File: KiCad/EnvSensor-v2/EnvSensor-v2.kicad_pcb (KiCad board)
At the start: 2 copper layers, 120 x 100 mm, 162 parts, among them J1 JTAG, J10 Conn_01x02, J2 Conn_01x02, J3 USB_B_Micro, J4 Conn_01x02, J5 Micro_SD_Card_Det, J6 Conn_01x02, J7 I2C, J8 HPMA115C0-003, J9 Conn_01x02, P1 USB_C_Plug_USB2.0, Q1 IRLML2502, Q2 Si3407DV, Q3 AUiRLR3110Z, Q4 AO6804A, SW1 SW_Push, SW2 Reset, SW3 SW_Push, SW4 SW_Push, SW5 SW_Push, SW6 Start, U1 STM32L451RCT6, U10 LTC3440, U11 MCP1826S-5.0, U12 MCP1825S-3.3, U13 ESP-12S, U2 E-Ink_Waveshare_4.2, U3 SCD30, U4 SCD40, U5 BME280, U6 AP9101CK, U7 MCP73843-4.2, U8 BME280-Module, U9 LM2735XMF, Y1 16Hz, Y2 32768/12.5pF

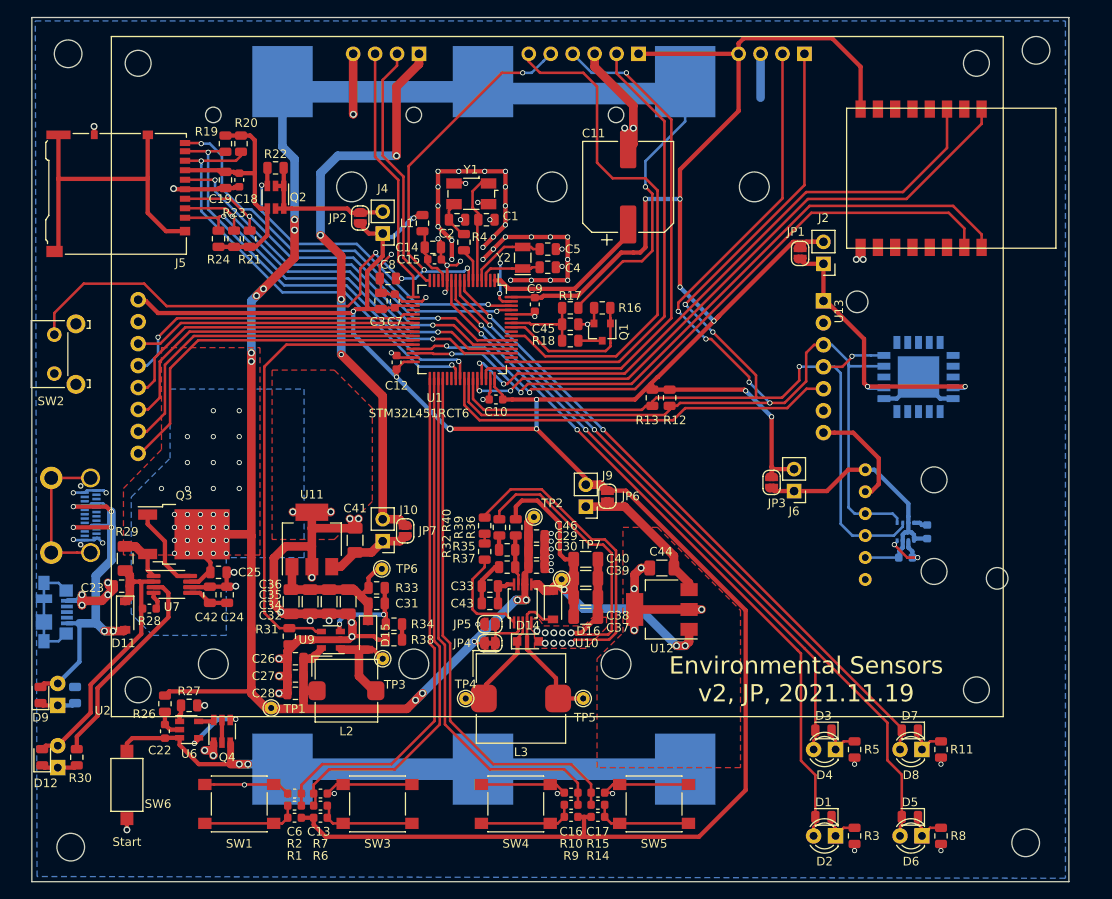
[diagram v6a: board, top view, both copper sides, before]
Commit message: Optimising ground pane
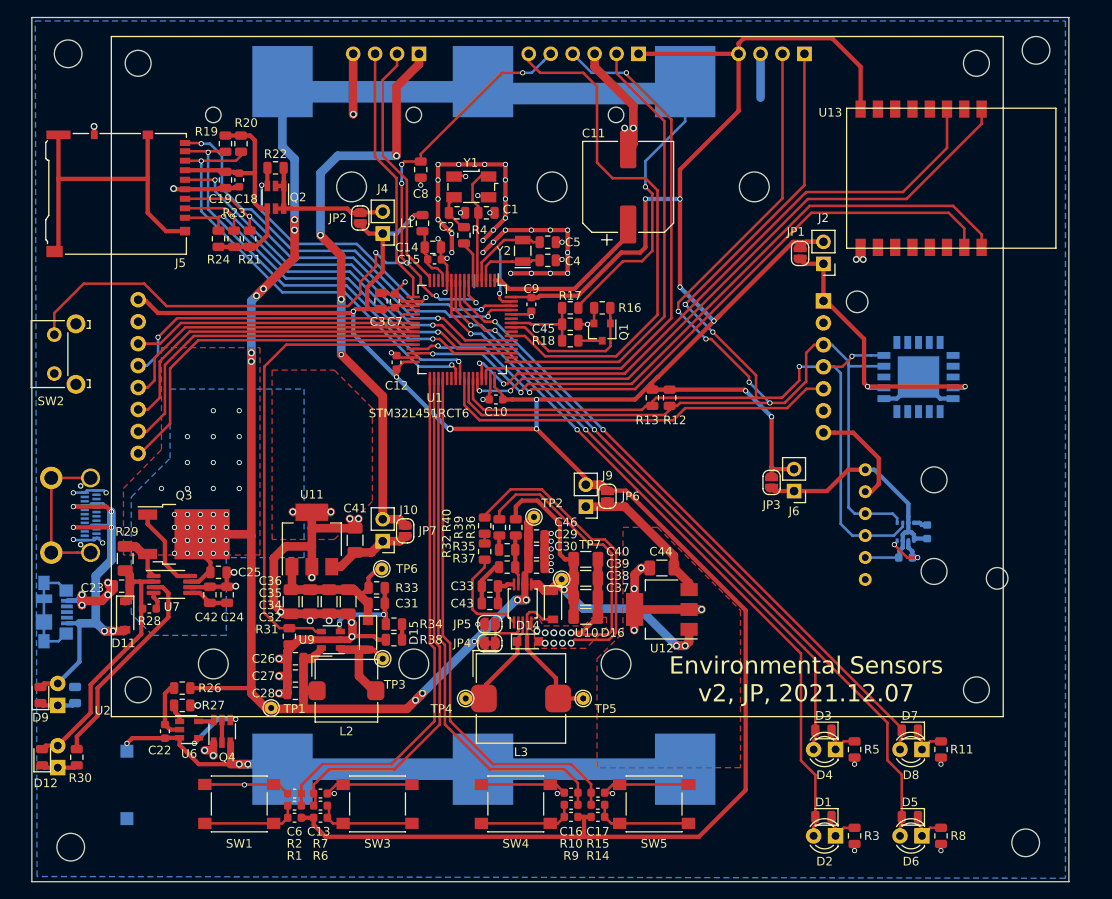
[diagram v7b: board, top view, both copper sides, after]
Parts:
- SW6: moved to B.Cu
- moved C8 13.2 mm to (95.0, 67.6), turned to 90 degrees
- moved R26 2.69 mm to (67.4, 127.6), turned to 180 degrees
- moved C1 0.80 mm to (102.6, 72.6)
- moved C2 0.80 mm to (99.2, 72.6)
- moved C4 0.80 mm to (109.7, 78.1)
- moved Y1 0.80 mm to (100.8, 69.6)
- moved C5 0.80 mm to (109.7, 76.0)
- moved R27 0.80 mm to (67.4, 129.6)
- moved R4 0.80 mm to (100.0, 75.2)
- moved Y2 0.80 mm to (106.8, 77.0)
- moved C9 0.40 mm to (107.8, 83.2)
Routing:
- net Net-(C22-Pad1): track 3.42 -> 6.85 mm
- net +BATT: track 245.1 -> 241.8 mm
- net GND: track 421.2 -> 418.1 mm, vias 107 -> 105
- net NRST: track 95.9 -> 98.6 mm, vias 5 -> 7
- net Net-(C4-Pad1): track 7.34 -> 8.14 mm
- net Net-(C5-Pad1): track 9.17 -> 9.97 mm
- net Net-(R4-Pad1): track 3.72 -> 4.52 mm
- net Net-(C1-Pad1): track 13.0 -> 13.8 mm
- net SDIO_DETECT: track 48.1 -> 48.8 mm
- net LED_1: track 81.8 -> 82.5 mm
- net LED_4: track 75.3 -> 76.0 mm
- net LED_3: track 85.5 -> 86.2 mm
- net LED_2: track 71.6 -> 72.3 mm
- net +3V3: track 372.1 -> 372.8 mm
- net -BATT: vias 2 -> 3
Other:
- board text added: "Environmental Sensors v2, JP, 2021.12.07"
- board text removed: "Environmental Sensors v2, JP, 2021.11.19"

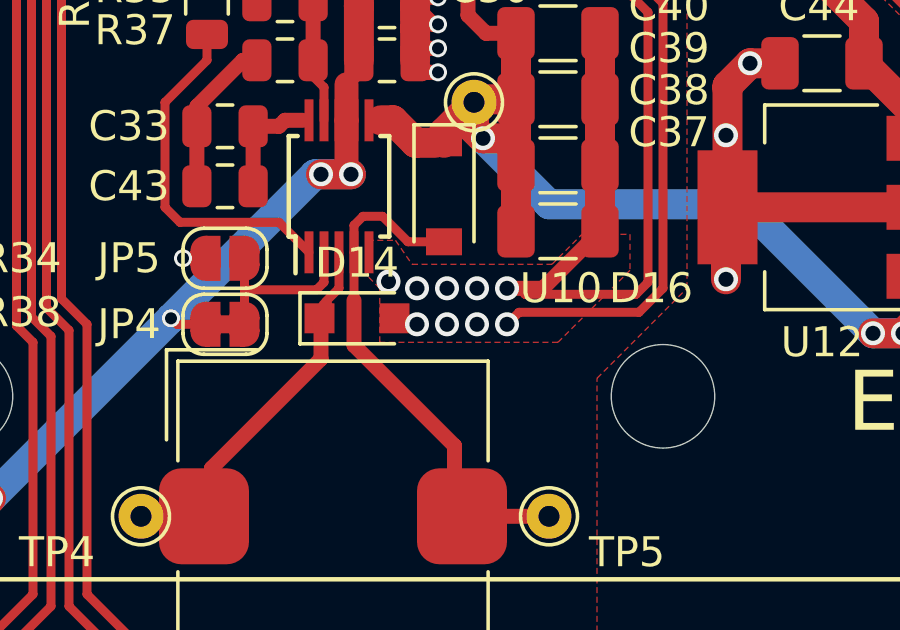
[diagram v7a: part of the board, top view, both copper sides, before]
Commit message: STM32CubeIDE/EnvSensorV2 introduced
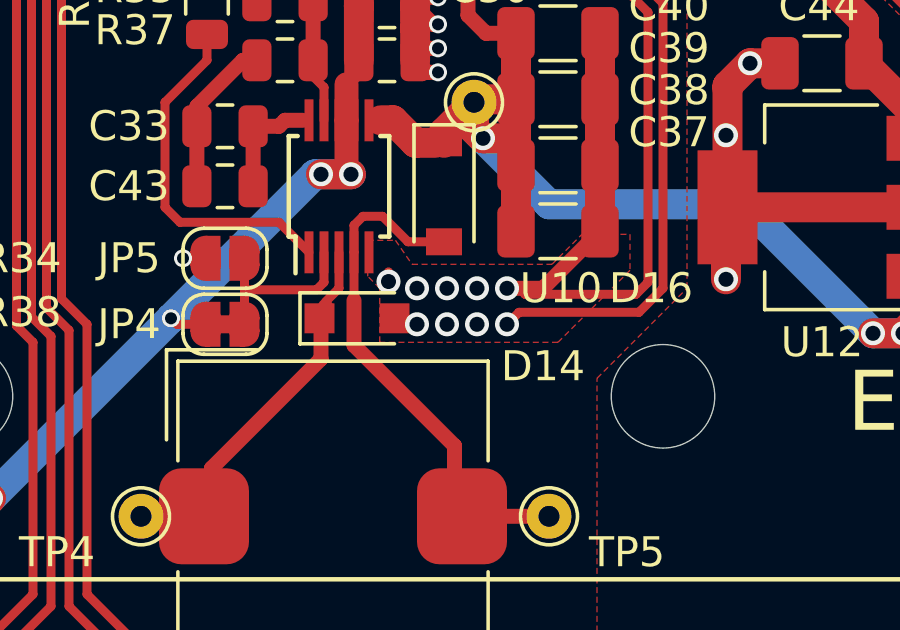
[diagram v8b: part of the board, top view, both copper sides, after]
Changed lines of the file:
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@@
   )
   (setup
-    (last_trace_width 0.5)
+    (last_trace_width 0.3)
     (user_trace_width 0.3)
     (user_trace_width 0.5)
@@
     (tags SOD-323)
     (attr smd)
-    (fp_text reference D14 (at 0 -1.85) (layer F.SilkS)
+    (fp_text reference D14 (at 6.2 1.6) (layer F.SilkS)
       (effects (font (size 1 1) (thickness 0.15)))
     )
@@
   (gr_line (start 170 50) (end 170 150) (layer Edge.Cuts) (width 0.05))
   (gr_line (start 50 50) (end 170 50) (layer Edge.Cuts) (width 0.05))
-  (segment (start 101.2 79.8) (end 101.2 81.2) (width 0.3) (layer B.Cu) (net 3))
   (segment (start 79 136.98) (end 102.2 136.98) (width 2.5) (layer B.Cu) (net 1))
   (segment (start 102.2 136.98) (end 125.6 136.98) (width 2.5) (layer B.Cu) (net 1))
@@
   (segment (start 120.6 78.2) (end 118.4 78.2) (width 0.3) (layer F.Cu) (net 2))
   (segment (start 68.3375 127.6) (end 75.4 127.6) (width 0.5) (layer F.Cu) (net 2))
+  (segment (start 101.2 79.8) (end 101.2 81.2) (width 0.3) (layer B.Cu) (net 3))
   (via (at 119.6 62.8) (size 0.8) (drill 0.5) (layers F.Cu B.Cu) (net 3))
   (via (at 119.7 120.9) (size 0.8) (drill 0.5) (layers F.Cu B.Cu) (net 3))
